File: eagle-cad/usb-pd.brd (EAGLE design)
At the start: 68.6 x 53.3 mm, 49 parts, among them Q1 CERAMIC_RESONATOR_SMD6M00G53Z, Q2 FDN352A, U1 ATMEGA328-AU

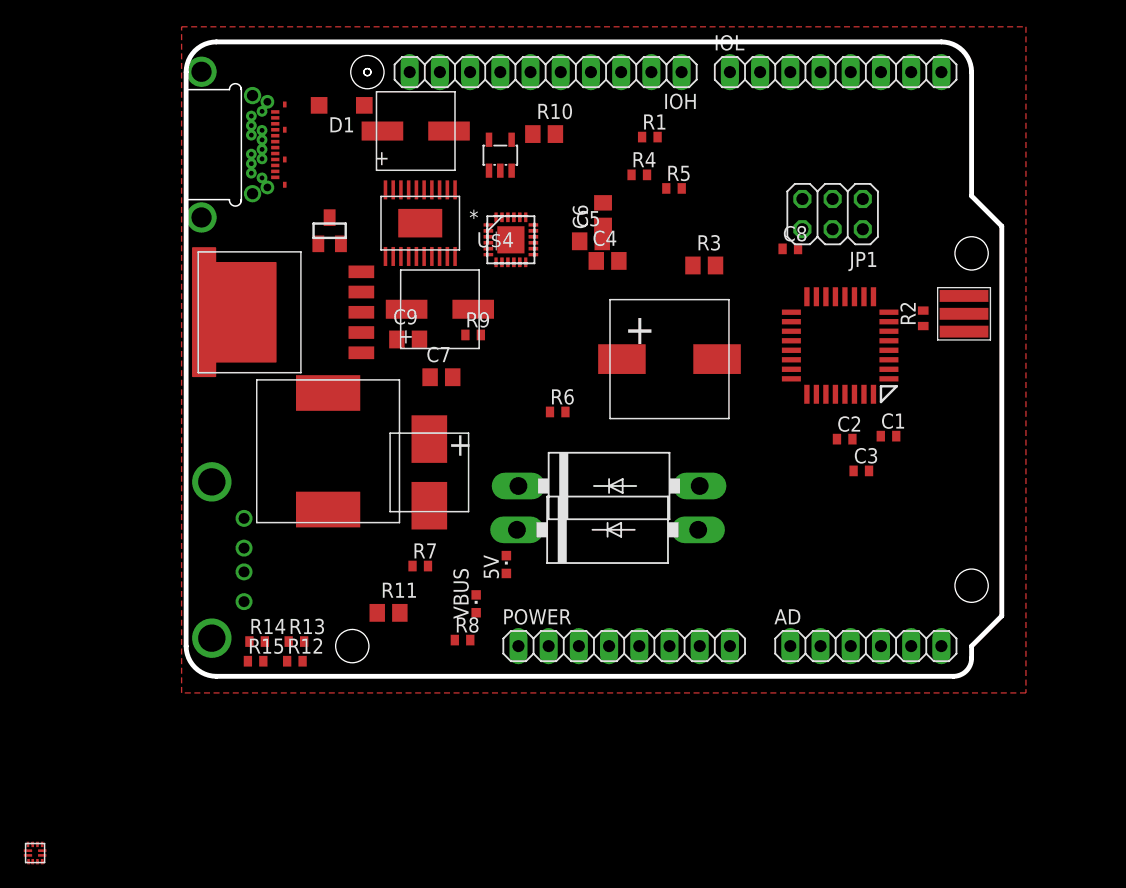
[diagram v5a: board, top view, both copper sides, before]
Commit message: Finished placement, started routing
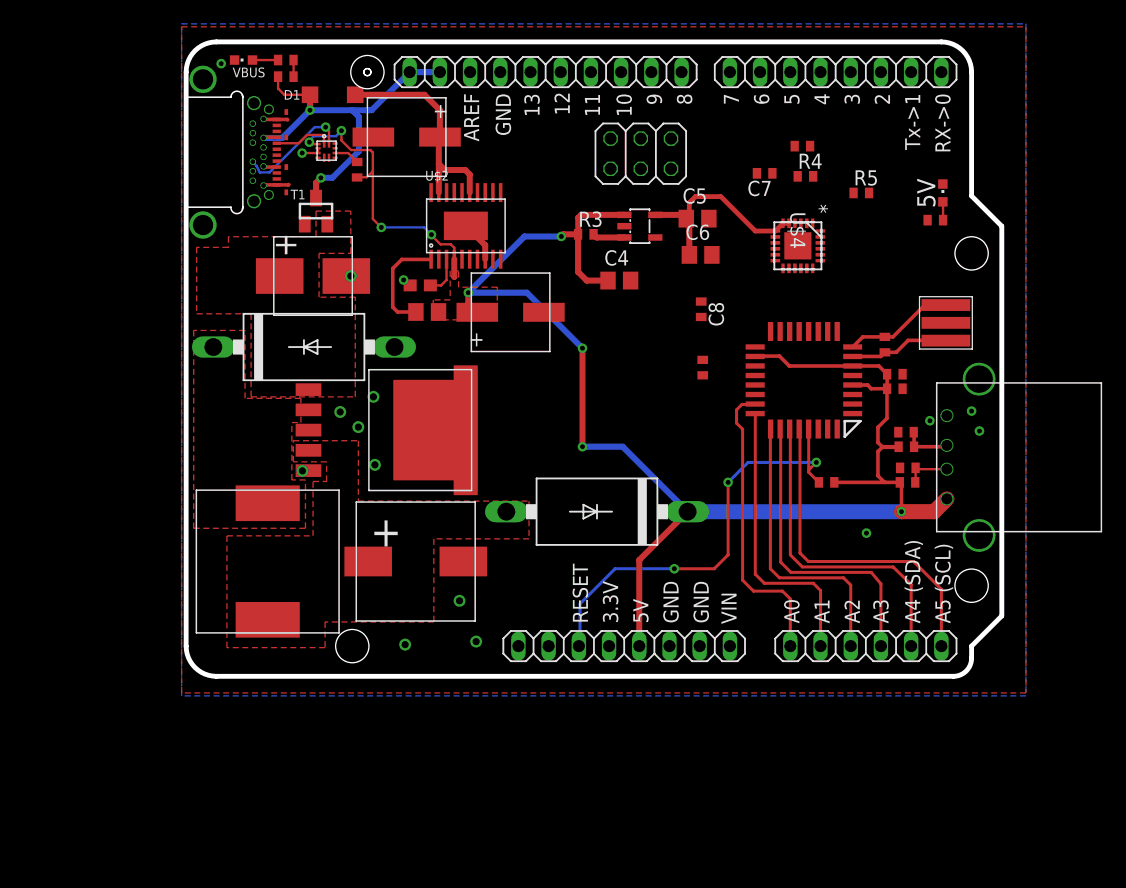
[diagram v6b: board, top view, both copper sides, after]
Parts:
- removed Q2: FDN352A, transistor-power:SUPER-SOT3
- added T1: FDN360P, transistor-power:SUPER-SOT3
- C7: device rcl:C0805 -> rcl:C0402
- C9: device rcl:C0805 -> rcl:C0603
- R11, R3: device rcl:R0805 -> rcl:R0402
- moved U$9 65.1 mm to (66.7, 18.4), turned to 90 degrees
- moved U$3 63.9 mm to (11.8, 44.2), turned to 270 degrees
- moved R15 57.6 mm to (60.6, 19.3), turned to 180 degrees
- moved R14 57.3 mm to (60.5, 20.5), turned to 180 degrees
- moved R12 53.7 mm to (60.7, 16.3), turned to 180 degrees
- moved R13 53.4 mm to (60.7, 17.5), turned to 180 degrees
- moved R11 52.4 mm to (51.8, 44.6), turned to 180 degrees
- moved R7 52.2 mm to (63.0, 38.4), turned to 180 degrees
- moved VBUS 49.7 mm to (4.83, 51.8), turned to 90 degrees
- moved R8 49.6 mm to (8.38, 50.4), turned to 180 degrees
- moved 5V 48.2 mm to (63.6, 40.6)
- moved R1 32.6 mm to (53.8, 16.3)
- moved C7 32.1 mm to (48.6, 42.3), turned to 180 degrees
- moved D2 28.2 mm to (9.91, 27.7)
- moved R9 28.0 mm to (8.38, 51.8)
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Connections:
- net AD0: now also AD.1
- net GND: now also U$2.P$21
- net IO2: now also T1.1; no longer Q2.1
- net N$1: now also T1.2; no longer Q2.3
- net VBUS: now also IOH.10, IOH.9, T1.3; no longer POWER.8, Q2.2
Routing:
- net +5V: track 0.00 -> 151.6 mm, vias 0 -> 9
- net RESET: track 0.00 -> 37.7 mm, vias 0 -> 3
- net VBUS: track 0.00 -> 34.3 mm, vias 0 -> 2
- net PD_SCL: track 0.00 -> 28.4 mm
- net PD_SDA: track 0.00 -> 27.0 mm
- net AD3: track 0.00 -> 25.7 mm
- net AD0: track 0.00 -> 24.9 mm
- net AD2: track 0.00 -> 24.3 mm
- net AD1: track 0.00 -> 24.2 mm
- net N$40: track 0.00 -> 19.1 mm
- net +3V3: track 0.00 -> 17.5 mm
- net GND: track 0.00 -> 10.2 mm, vias 0 -> 16
- net N$6: track 0.00 -> 9.70 mm, vias 0 -> 1
- net N$3: track 0.00 -> 9.33 mm
- net N$13: track 0.00 -> 8.91 mm
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- added copper zone on layer 1, net +5V
- added copper zone on layer 16, net GND
- added copper zone on layer 1, net N$1
- added copper zone on layer 1, net N$15
- added copper zone on layer 1, net N$9
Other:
- board text added: "10"
- board text added: "11"
- board text added: "12"
- board text added: "13"
- board text added: "2"
- board text added: "3"
- board text added: "3.3V"
- board text added: "4"
- board text added: "5"
- board text added: "5V"
- board text added: "6"
- board text added: "7"
- board text added: "8"
- board text added: "9"
- board text added: "A0"
- board text added: "A1"
- board text added: "A2"
- board text added: "A3"
- board text added: "A4 (SDA)"
- board text added: "A5 (SCL)"
- board text added: "AREF"
- board text added: "GND"
- board text added: "RESET"
- board text added: "RX->0"
- board text added: "Tx->1"
- board text added: "VIN"

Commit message: Entire-board-routed, rev-1. This is going to need a lot of revisions.
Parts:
- moved R11 24.0 mm to (34.7, 27.7), turned to 270 degrees
- moved R5 23.5 mm to (42.1, 22.3)
- moved R4 23.4 mm to (42.1, 20.9)
- moved C8 21.3 mm to (27.0, 44.5), turned to 180 degrees
- moved C7 15.6 mm to (61.6, 33.6)
- moved U$4 6.45 mm to (57.9, 36.0), turned to 180 degrees
- moved JP1 3.54 mm to (36.3, 40.9)
- moved C2 2.48 mm to (61.7, 25.5), turned to 270 degrees
- moved C3 2.42 mm to (45.5, 24.6), turned to 270 degrees
- moved 5V 2.21 mm to (61.7, 41.7)
- moved C4 1.94 mm to (35.0, 32.0)
- moved C5 1.94 mm to (41.6, 37.2)
- moved R3 1.94 mm to (32.2, 35.8)
- moved U$5 1.94 mm to (36.7, 36.5)
- moved C6 1.72 mm to (41.6, 34.9)
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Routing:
- net IO2: track 0.00 -> 97.2 mm, vias 0 -> 9
- net USB+: track 0.00 -> 73.1 mm, vias 0 -> 3
- net USB-: track 0.00 -> 71.0 mm, vias 0 -> 2
- net PD_SCL: track 28.4 -> 92.9 mm, vias 0 -> 3
- net +5V: track 151.6 -> 215.2 mm, vias 9 -> 13
- net PD_SDA: track 27.0 -> 83.8 mm, vias 0 -> 3
- net RESET: track 37.7 -> 92.0 mm, vias 3 -> 6
- net +3V3: track 17.5 -> 64.8 mm, vias 0 -> 4
- net IO4: track 0.00 -> 43.2 mm, vias 0 -> 2
- net USB_TX: track 0.00 -> 42.3 mm, vias 0 -> 3
- net MISO: track 0.00 -> 41.1 mm, vias 0 -> 2
- net IO3: track 0.00 -> 41.1 mm, vias 0 -> 2
- net USB_RX: track 0.00 -> 40.1 mm, vias 0 -> 3
- net AREF: track 0.00 -> 39.5 mm, vias 0 -> 2
- net SCLK: track 0.00 -> 37.6 mm, vias 0 -> 1
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
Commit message: Added stitching vias and played with ground planes
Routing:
- net GND: track 20.8 -> 17.3 mm, vias 28 -> 74
- net MISO: track 41.1 -> 43.1 mm
- net AREF: track 39.5 -> 37.8 mm
- net SS: track 29.1 -> 27.7 mm
- net MOSI: track 33.5 -> 34.5 mm
- net RESET: track 92.0 -> 92.7 mm
- net IO2: track 97.2 -> 96.6 mm
